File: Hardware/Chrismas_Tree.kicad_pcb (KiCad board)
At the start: 2 copper layers, 264.4 x 368.3 mm, 207 parts, among them J1 DNP, J2 USB_B_Micro, Q1 BC548, U1 PIC18F23K22

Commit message: Added mounting holes to schematic.
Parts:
- removed REF** (x6): MountingHole_4.5mm_Pad, MountingHole:MountingHole_4.5mm_Pad
- added H1: Hole, MountingHole:MountingHole_4.5mm_Pad, F.Cu at (43.7, 40.6)
- added H2: Hole, MountingHole:MountingHole_4.5mm_Pad, F.Cu at (43.7, 209.8)
- added H3: Hole, MountingHole:MountingHole_4.5mm_Pad, F.Cu at (43.7, 379.0)
- added H4: Hole, MountingHole:MountingHole_4.5mm_Pad, F.Cu at (278.1, 379.0)
- added H5: Hole, MountingHole:MountingHole_4.5mm_Pad, F.Cu at (278.1, 209.8)
- added H6: Hole, MountingHole:MountingHole_4.5mm_Pad, F.Cu at (278.1, 40.6)
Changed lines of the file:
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@@
   )
   (setup
-    (last_trace_width 1.5)
+    (last_trace_width 0.25)
     (user_trace_width 0.4)
     (user_trace_width 1)
@@
   )
   (module MountingHole:MountingHole_4.5mm_Pad (layer F.Cu)
+    (at 278.13 40.64)
+    (descr "Mounting Hole 4.5mm")
+    (tags "mounting hole 4.5mm")
+    (attr virtual)
+    (fp_text reference H6 (at 0 -5.5) (layer F.SilkS)
+      (effects (font (size 1 1) (thickness 0.15)))
+    )
+    (fp_text value Hole (at 0 5.5) (layer F.Fab)
+      (effects (font (size 1 1) (thickness 0.15)))
+    )
+    (fp_circle (center 0 0) (end 4.75 0) (layer F.CrtYd) (width 0.05))
+    (fp_circle (center 0 0) (end 4.5 0) (layer Cmts.User) (width 0.15))
+    (fp_text user %R (at 0.3 0) (layer F.Fab)
+      (effects (font (size 1 1) (thickness 0.15)))
+    )
+    (pad 1 thru_hole circle (at 0 0) (size 9 9) (drill 4.5) (layers *.Cu *.Mask)
+      (net 25 GND))
+  )
+  (module MountingHole:MountingHole_4.5mm_Pad (layer F.Cu)
+    (at 278.13 209.804)
+    (descr "Mounting Hole 4.5mm")
+    (tags "mounting hole 4.5mm")
+    (attr virtual)
+    (fp_text reference H5 (at 0 -5.5) (layer F.SilkS)
+      (effects (font (size 1 1) (thickness 0.15)))
+    )
+    (fp_text value Hole (at 0 5.5) (layer F.Fab)
+      (effects (font (size 1 1) (thickness 0.15)))
+    )
+    (fp_circle (center 0 0) (end 4.75 0) (layer F.CrtYd) (width 0.05))
+    (fp_circle (center 0 0) (end 4.5 0) (layer Cmts.User) (width 0.15))
+    (fp_text user %R (at 0.3 0) (layer F.Fab)
+      (effects (font (size 1 1) (thickness 0.15)))
+    )
+    (pad 1 thru_hole circle (at 0 0) (size 9 9) (drill 4.5) (layers *.Cu *.Mask)
+      (net 25 GND))
+  )
+  (module MountingHole:MountingHole_4.5mm_Pad (layer F.Cu)
     (at 278.13 378.968)
     (descr "Mounting Hole 4.5mm")
     (tags "mounting hole 4.5mm")
     (attr virtual)
-    (fp_text reference REF** (at 0 -5.5) (layer F.SilkS) hide
-      (effects (font (size 1 1) (thickness 0.15)))
-    )
-    (fp_text value MountingHole_4.5mm_Pad (at 0 5.5) (layer F.Fab)
-      (effects (font (size 1 1) (thickness 0.15)))
-    )
-    (fp_text user %R (at 0.3 0) (layer F.Fab)
-      (effects (font (size 1 1) (thickness 0.15)))
-    )
-    (fp_circle (center 0 0) (end 4.5 0) (layer Cmts.User) (width 0.15))
-    (fp_circle (center 0 0) (end 4.75 0) (layer F.CrtYd) (width 0.05))
-    (pad 1 thru_hole circle (at 0 0) (size 9 9) (drill 4.5) (layers *.Cu *.Mask))
-  )
-  (module MountingHole:MountingHole_4.5mm_Pad (layer F.Cu)
-    (at 278.13 209.804)
-    (descr "Mounting Hole 4.5mm")
-    (tags "mounting hole 4.5mm")
-    (attr virtual)
-    (fp_text reference REF** (at 0 -5.5) (layer F.SilkS) hide
-      (effects (font (size 1 1) (thickness 0.15)))
-    )
-    (fp_text value MountingHole_4.5mm_Pad (at 0 5.5) (layer F.Fab)
-      (effects (font (size 1 1) (thickness 0.15)))
-    )
-    (fp_circle (center 0 0) (end 4.75 0) (layer F.CrtYd) (width 0.05))
-    (fp_circle (center 0 0) (end 4.5 0) (layer Cmts.User) (width 0.15))
-    (fp_text user %R (at 0.3 0) (layer F.Fab)
-      (effects (font (size 1 1) (thickness 0.15)))
-    )
-    (pad 1 thru_hole circle (at 0 0) (size 9 9) (drill 4.5) (layers *.Cu *.Mask))
-  )
-  (module MountingHole:MountingHole_4.5mm_Pad (layer F.Cu)
-    (at 278.13 40.64)
-    (descr "Mounting Hole 4.5mm")
-    (tags "mounting hole 4.5mm")
-    (attr virtual)
-    (fp_text reference REF** (at 0 -5.5) (layer F.SilkS) hide
-      (effects (font (size 1 1) (thickness 0.15)))
-    )
-    (fp_text value MountingHole_4.5mm_Pad (at 0 5.5) (layer F.Fab)
-      (effects (font (size 1 1) (thickness 0.15)))
-    )
-    (fp_text user %R (at 0.3 0) (layer F.Fab)
-      (effects (font (size 1 1) (thickness 0.15)))
-    )
-    (fp_circle (center 0 0) (end 4.5 0) (layer Cmts.User) (width 0.15))
-    (fp_circle (center 0 0) (end 4.75 0) (layer F.CrtYd) (width 0.05))
-    (pad 1 thru_hole circle (at 0 0) (size 9 9) (drill 4.5) (layers *.Cu *.Mask))
+    (fp_text reference H4 (at 0 -5.5) (layer F.SilkS)
+      (effects (font (size 1 1) (thickness 0.15)))
+    )
+    (fp_text value Hole (at 0 5.5) (layer F.Fab)
+      (effects (font (size 1 1) (thickness 0.15)))
+    )
+    (fp_circle (center 0 0) (end 4.75 0) (layer F.CrtYd) (width 0.05))
+    (fp_circle (center 0 0) (end 4.5 0) (layer Cmts.User) (width 0.15))
+    (fp_text user %R (at 0.3 0) (layer F.Fab)
+      (effects (font (size 1 1) (thickness 0.15)))
+    )
+    (pad 1 thru_hole circle (at 0 0) (size 9 9) (drill 4.5) (layers *.Cu *.Mask)
+      (net 25 GND))
+  )
+  (module MountingHole:MountingHole_4.5mm_Pad (layer F.Cu)
+    (at 43.688 378.968)
+    (descr "Mounting Hole 4.5mm")
+    (tags "mounting hole 4.5mm")
+    (attr virtual)
+    (fp_text reference H3 (at 0 -5.5) (layer F.SilkS)
+      (effects (font (size 1 1) (thickness 0.15)))
+    )
+    (fp_text value Hole (at 0 5.5) (layer F.Fab)
+      (effects (font (size 1 1) (thickness 0.15)))
+    )
+    (fp_circle (center 0 0) (end 4.75 0) (layer F.CrtYd) (width 0.05))
+    (fp_circle (center 0 0) (end 4.5 0) (layer Cmts.User) (width 0.15))
+    (fp_text user %R (at 0.3 0) (layer F.Fab)
+      (effects (font (size 1 1) (thickness 0.15)))
+    )
+    (pad 1 thru_hole circle (at 0 0) (size 9 9) (drill 4.5) (layers *.Cu *.Mask)
+      (net 25 GND))
+  )
+  (module MountingHole:MountingHole_4.5mm_Pad (layer F.Cu)
+    (at 43.688 209.804)
+    (descr "Mounting Hole 4.5mm")
+    (tags "mounting hole 4.5mm")
+    (attr virtual)
+    (fp_text reference H2 (at 0 -5.5) (layer F.SilkS)
+      (effects (font (size 1 1) (thickness 0.15)))
+    )
+    (fp_text value Hole (at 0 5.5) (layer F.Fab)
+      (effects (font (size 1 1) (thickness 0.15)))
+    )
+    (fp_circle (center 0 0) (end 4.75 0) (layer F.CrtYd) (width 0.05))
+    (fp_circle (center 0 0) (end 4.5 0) (layer Cmts.User) (width 0.15))
+    (fp_text user %R (at 0.3 0) (layer F.Fab)
+      (effects (font (size 1 1) (thickness 0.15)))
+    )
+    (pad 1 thru_hole circle (at 0 0) (size 9 9) (drill 4.5) (layers *.Cu *.Mask)
+      (net 25 GND))
   )
   (module MountingHole:MountingHole_4.5mm_Pad (layer F.Cu)
@@
     (tags "mounting hole 4.5mm")
     (attr virtual)
-    (fp_text reference REF** (at 0 -5.5) (layer F.SilkS) hide
-      (effects (font (size 1 1) (thickness 0.15)))
-    )
-    (fp_text value MountingHole_4.5mm_Pad (at 0 5.5) (layer F.Fab)
-      (effects (font (size 1 1) (thickness 0.15)))
-    )
-    (fp_circle (center 0 0) (end 4.75 0) (layer F.CrtYd) (width 0.05))
-    (fp_circle (center 0 0) (end 4.5 0) (layer Cmts.User) (width 0.15))
-    (fp_text user %R (at 0.3 0) (layer F.Fab)
-      (effects (font (size 1 1) (thickness 0.15)))
-    )
-    (pad 1 thru_hole circle (at 0 0) (size 9 9) (drill 4.5) (layers *.Cu *.Mask))
-  )
-  (module MountingHole:MountingHole_4.5mm_Pad (layer F.Cu)
-    (at 43.688 209.804)
-    (descr "Mounting Hole 4.5mm")
-    (tags "mounting hole 4.5mm")
-    (attr virtual)
-    (fp_text reference REF** (at 0 -5.5) (layer F.SilkS) hide
-      (effects (font (size 1 1) (thickness 0.15)))
-    )
-    (fp_text value MountingHole_4.5mm_Pad (at 0 5.5) (layer F.Fab)
-      (effects (font (size 1 1) (thickness 0.15)))
-    )
-    (fp_text user %R (at 0.3 0) (layer F.Fab)
-      (effects (font (size 1 1) (thickness 0.15)))
-    )
-    (fp_circle (center 0 0) (end 4.5 0) (layer Cmts.User) (width 0.15))
-    (fp_circle (center 0 0) (end 4.75 0) (layer F.CrtYd) (width 0.05))
-    (pad 1 thru_hole circle (at 0 0) (size 9 9) (drill 4.5) (layers *.Cu *.Mask))
-  )
-  (module MountingHole:MountingHole_4.5mm_Pad (layer F.Cu)
-    (at 43.688 378.968)
-    (descr "Mounting Hole 4.5mm")
-    (tags "mounting hole 4.5mm")
-    (attr virtual)
-    (fp_text reference REF** (at 0 -5.5) (layer F.SilkS) hide
-      (effects (font (size 1 1) (thickness 0.15)))
-    )
-    (fp_text value MountingHole_4.5mm_Pad (at 0 5.5) (layer F.Fab)
-      (effects (font (size 1 1) (thickness 0.15)))
-    )
-    (fp_circle (center 0 0) (end 4.75 0) (layer F.CrtYd) (width 0.05))
-    (fp_circle (center 0 0) (end 4.5 0) (layer Cmts.User) (width 0.15))
-    (fp_text user %R (at 0.3 0) (layer F.Fab)
-      (effects (font (size 1 1) (thickness 0.15)))
-    )
-    (pad 1 thru_hole circle (at 0 0) (size 9 9) (drill 4.5) (layers *.Cu *.Mask))
+    (fp_text reference H1 (at 0 -5.5) (layer F.SilkS)
+      (effects (font (size 1 1) (thickness 0.15)))
+    )
+    (fp_text value Hole (at 0 5.5) (layer F.Fab)
+      (effects (font (size 1 1) (thickness 0.15)))
+    )
+    (fp_circle (center 0 0) (end 4.75 0) (layer F.CrtYd) (width 0.05))
+    (fp_circle (center 0 0) (end 4.5 0) (layer Cmts.User) (width 0.15))
+    (fp_text user %R (at 0.3 0) (layer F.Fab)
+      (effects (font (size 1 1) (thickness 0.15)))
+    )
+    (pad 1 thru_hole circle (at 0 0) (size 9 9) (drill 4.5) (layers *.Cu *.Mask)
+      (net 25 GND))
   )
   (module Connector_USB:USB_Micro-B_Molex-105017-0001 (layer B.Cu)

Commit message: Updated schematic and PCB to use microcontroller hardware PWMs to control fairy lights by color and star instead of all light bulbs separately.
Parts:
- added Q2: 2N2222A, Package_TO_SOT_THT:TO-18-3, B.Cu at (160.0, 171.4)
- added Q3: 2N2222A, Package_TO_SOT_THT:TO-18-3, B.Cu at (124.5, 289.6)
- added Q4: 2N2222A, Package_TO_SOT_THT:TO-18-3, B.Cu at (209.6, 289.6)
- added R100: 820, Resistor_THT:R_Axial_DIN0207_L6.3mm_D2.5mm_P7.62mm_Horizontal, B.Cu at (168.9, 204.5)
- added R101: 820, Resistor_THT:R_Axial_DIN0207_L6.3mm_D2.5mm_P7.62mm_Horizontal, B.Cu at (207.0, 297.2)
- added R99: 820, Resistor_THT:R_Axial_DIN0207_L6.3mm_D2.5mm_P7.62mm_Horizontal, B.Cu at (138.4, 290.8)
- D82, D87, D91: value LED -> Blue
- D83, D84, D88, D89: value LED -> Red
- D85, D86, D90: value LED -> Yellow
- D92, D93, D94, D95: value RED -> Yellow
- Q1: value BC548 -> 2N2222A; footprint Package_TO_SOT_THT:TO-92_Inline -> Package_TO_SOT_THT:TO-18-3
- R96: value 220 -> 820
- moved R82 92.5 mm to (141.0, 142.2), turned to 0 degrees
- moved R83 83.0 mm to (181.6, 142.2), turned to 180 degrees
- moved R89 76.8 mm to (246.4, 299.7), turned to 180 degrees
- moved R90 72.9 mm to (106.7, 312.4), turned to 90 degrees
- moved R88 69.5 mm to (95.2, 294.6), turned to 0 degrees
- moved R91 58.0 mm to (217.2, 312.4), turned to 90 degrees
- moved R86 45.3 mm to (111.8, 271.8), turned to 0 degrees
- moved R84 44.5 mm to (138.4, 193.0), turned to 0 degrees
- moved R85 41.4 mm to (191.8, 198.1), turned to 180 degrees
- moved R87 29.8 mm to (201.9, 257.8), turned to 180 degrees
- moved R96 20.6 mm to (175.3, 204.5)
- moved D90 4.93 mm to (101.6, 328.9), turned to 180 degrees
- moved D88 4.64 mm to (59.7, 318.8), turned to 180 degrees
- moved D84 4.10 mm to (96.5, 188.0), turned to 180 degrees
- moved D86 3.06 mm to (80.0, 251.5), turned to 90 degrees
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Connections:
- D82 pad 1: GND -> Net-(D82-Pad1)
- D82 pad 2: Net-(D82-Pad2) -> +5V
- D83 pad 1: GND -> Net-(D83-Pad1)
- D83 pad 2: Net-(D83-Pad2) -> +5V
- D84 pad 1: GND -> Net-(D84-Pad1)
- D84 pad 2: Net-(D84-Pad2) -> +5V
- D85 pad 1: GND -> Net-(D85-Pad1)
- D85 pad 2: Net-(D85-Pad2) -> +5V
- D86 pad 1: GND -> Net-(D86-Pad1)
- D86 pad 2: Net-(D86-Pad2) -> +5V
- D87 pad 1: GND -> Net-(D87-Pad1)
- D87 pad 2: Net-(D87-Pad2) -> +5V
- D88 pad 1: GND -> Net-(D88-Pad1)
- D88 pad 2: Net-(D88-Pad2) -> +5V
- D89 pad 1: GND -> Net-(D89-Pad1)
- D89 pad 2: Net-(D89-Pad2) -> +5V
- D90 pad 1: GND -> Net-(D90-Pad1)
- D90 pad 2: Net-(D90-Pad2) -> +5V
- D91 pad 1: GND -> Net-(D91-Pad1)
- D91 pad 2: Net-(D91-Pad2) -> +5V
- Q1 pad 1: Net-(D92-Pad1) -> GND
- Q1 pad 3: GND -> Net-(D92-Pad1)
- R82 pad 1: /Light bulbs/Bulb_0 -> Net-(D82-Pad1)
- R82 pad 2: Net-(D82-Pad2) -> Net-(Q4-Pad3)
- R83 pad 1: /Light bulbs/Bulb_9 -> Net-(D83-Pad1)
- R83 pad 2: Net-(D83-Pad2) -> Net-(Q2-Pad3)
- R84 pad 1: /Light bulbs/Bulb_1 -> Net-(D84-Pad1)
- R84 pad 2: Net-(D84-Pad2) -> Net-(Q2-Pad3)
- R85 pad 1: /Light bulbs/Bulb_8 -> Net-(D85-Pad1)
- R85 pad 2: Net-(D85-Pad2) -> Net-(Q3-Pad3)
- R86 pad 1: /Light bulbs/Bulb_2 -> Net-(D86-Pad1)
- R86 pad 2: Net-(D86-Pad2) -> Net-(Q3-Pad3)
- R87 pad 1: /Light bulbs/Bulb_7 -> Net-(D87-Pad1)
- R87 pad 2: Net-(D87-Pad2) -> Net-(Q4-Pad3)
- R88 pad 1: /Light bulbs/Bulb_3 -> Net-(D88-Pad1)
- R88 pad 2: Net-(D88-Pad2) -> Net-(Q2-Pad3)
- R89 pad 1: /Light bulbs/Bulb_6 -> Net-(D89-Pad1)
- R89 pad 2: Net-(D89-Pad2) -> Net-(Q2-Pad3)
- R90 pad 1: /Light bulbs/Bulb_4 -> Net-(D90-Pad1)
- R90 pad 2: Net-(D90-Pad2) -> Net-(Q3-Pad3)
- R91 pad 1: /Light bulbs/Bulb_5 -> Net-(D91-Pad1)
- R91 pad 2: Net-(D91-Pad2) -> Net-(Q4-Pad3)
- R96 pad 2: /Light bulbs/Star -> Net-(R96-Pad2)
- U1 pad 10: /Light bulbs/Bulb_3 -> Net-(U1-Pad10)
- U1 pad 11: /Light bulbs/Bulb_2 -> Net-(U1-Pad11)
- U1 pad 12: /Light bulbs/Bulb_1 -> Net-(R100-Pad2)
- U1 pad 13: /Light bulbs/Bulb_0 -> Net-(R96-Pad2)
- U1 pad 14: /Light bulbs/Star -> Net-(U1-Pad14)
- U1 pad 15: /Light bulbs/Bulb_9 -> Net-(U1-Pad15)
- U1 pad 16: /Light bulbs/Bulb_8 -> Net-(U1-Pad16)
- U1 pad 17: /Light bulbs/Bulb_7 -> Net-(U1-Pad17)
- U1 pad 25: /Light bulbs/Bulb_6 -> Net-(U1-Pad25)
- U1 pad 26: /Light bulbs/Bulb_5 -> Net-(R101-Pad2)
- U1 pad 9: /Light bulbs/Bulb_4 -> Net-(U1-Pad9)
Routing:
- net Net-(Q2-Pad3): track 0.00 -> 333.5 mm
- net +5V: track 1502.3 -> 1807.4 mm
- net Net-(Q4-Pad3): track 0.00 -> 211.7 mm
- net Net-(Q3-Pad3): track 0.00 -> 166.8 mm
- net Net-(D82-Pad2): track 131.1 -> 0.00 mm
- net Net-(D88-Pad2): track 119.9 -> 0.00 mm
- net Net-(D83-Pad2): track 114.3 -> 0.00 mm
- net Net-(D89-Pad2): track 103.7 -> 0.00 mm
- net Net-(D90-Pad2): track 95.7 -> 0.00 mm
- net Net-(D85-Pad2): track 89.0 -> 0.00 mm
- net Net-(D91-Pad2): track 77.3 -> 0.00 mm
- net Net-(D87-Pad2): track 72.2 -> 0.00 mm
- net Net-(D84-Pad2): track 70.2 -> 0.00 mm
- net Net-(R101-Pad2): track 0.00 -> 60.4 mm
- net Net-(D86-Pad2): track 59.4 -> 0.00 mm
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
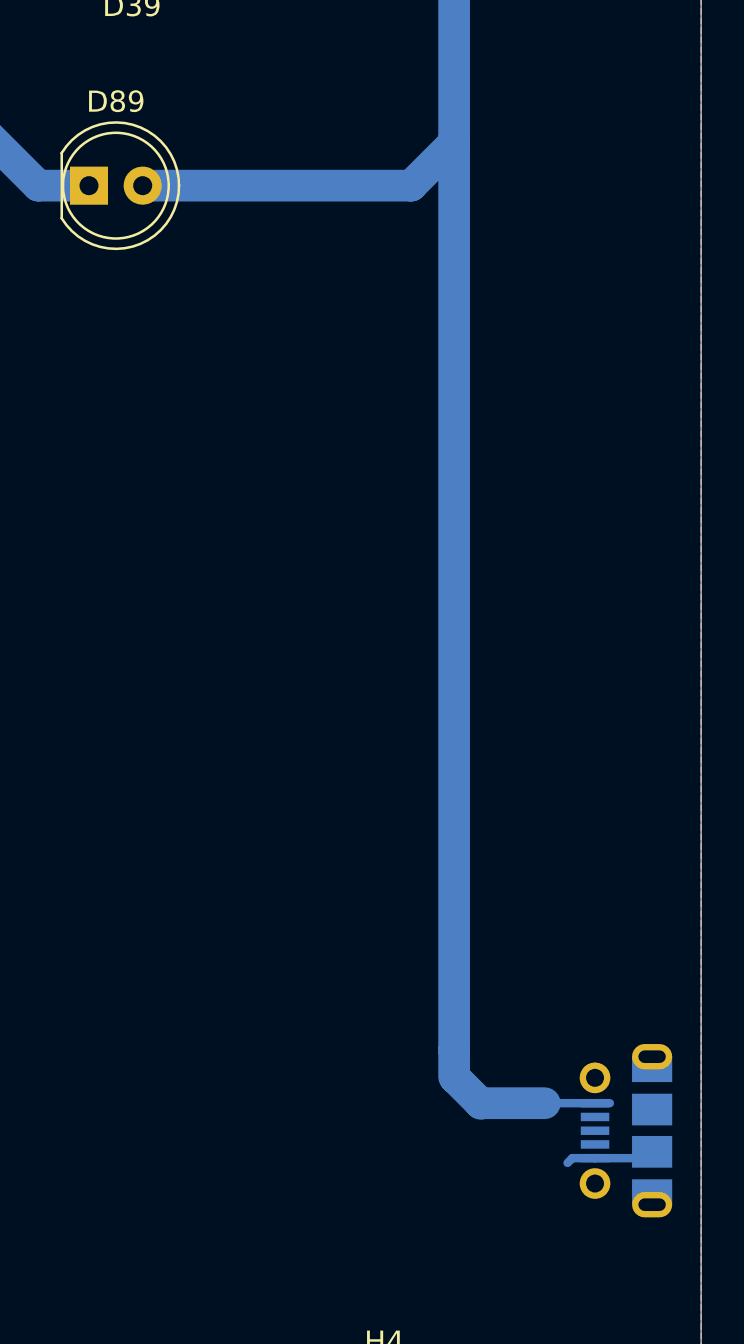
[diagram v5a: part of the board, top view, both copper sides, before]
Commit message: Replaced USB micro B connector by a more robust USB B one.
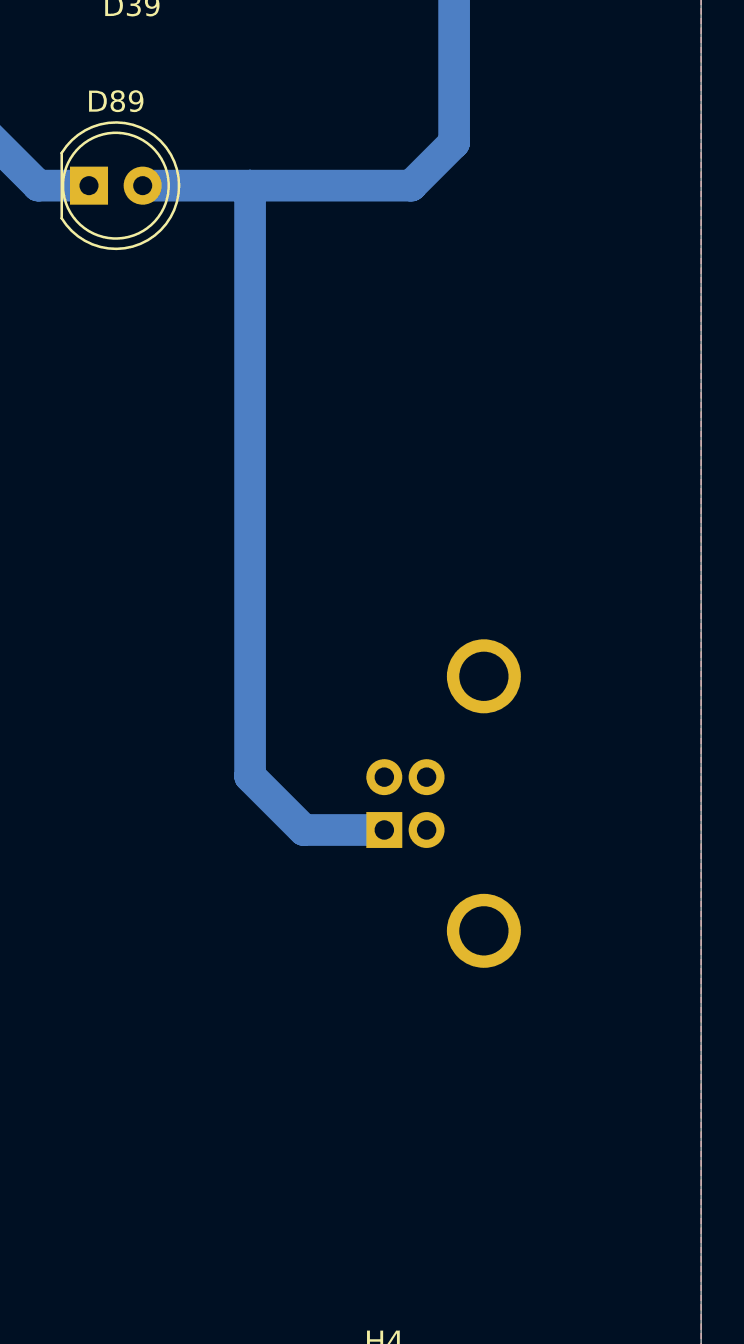
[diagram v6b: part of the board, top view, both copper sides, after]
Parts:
- J2: value USB_B_Micro -> USB_B; footprint Connector_USB:USB_Micro-B_Molex-105017-0001 -> Connector_USB:USB_B_OST_USB-B1HSxx_Horizontal
- moved J2 18.2 mm to (278.1, 349.2), turned to 0 degrees
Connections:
- J2 pad 4: Net-(J2-Pad4) -> GND
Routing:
- net +5V: track 1807.4 -> 1791.3 mm
- net GND: track 24.8 -> 20.6 mm
